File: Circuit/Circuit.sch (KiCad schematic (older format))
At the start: 103 parts, among them SW1 SW_Push, SW10 SW_Push, SW11 SW_Push, SW12 SW_Push, SW13 SW_Push, SW14 SW_Push, SW15 SW_Push, SW16 SW_Push, SW17 SW_Push, SW2 SW_Push, SW3 SW_Push, SW4 SW_Push, SW5 SW_Push, SW6 SW_Push, SW7 SW_Push, SW8 SW_Push, SW9 SW_Push, U1 AD9837, U2 MAX7219

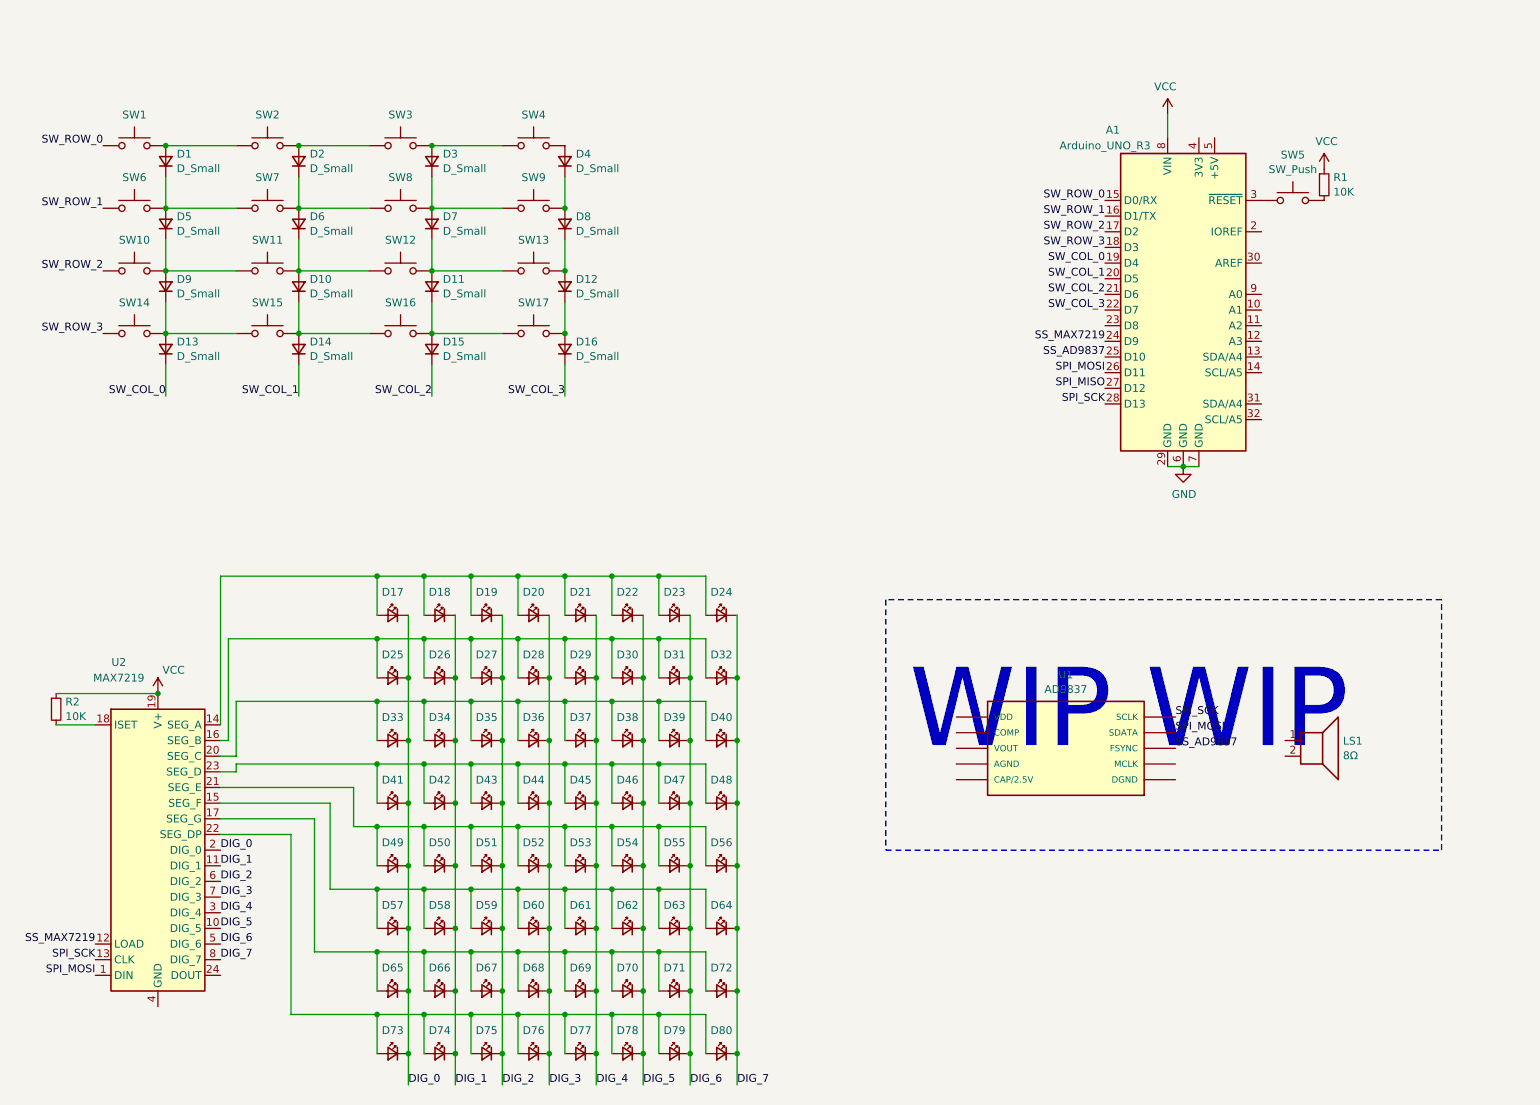
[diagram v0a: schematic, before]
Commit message: Make progress with audio and start laying out PCB.
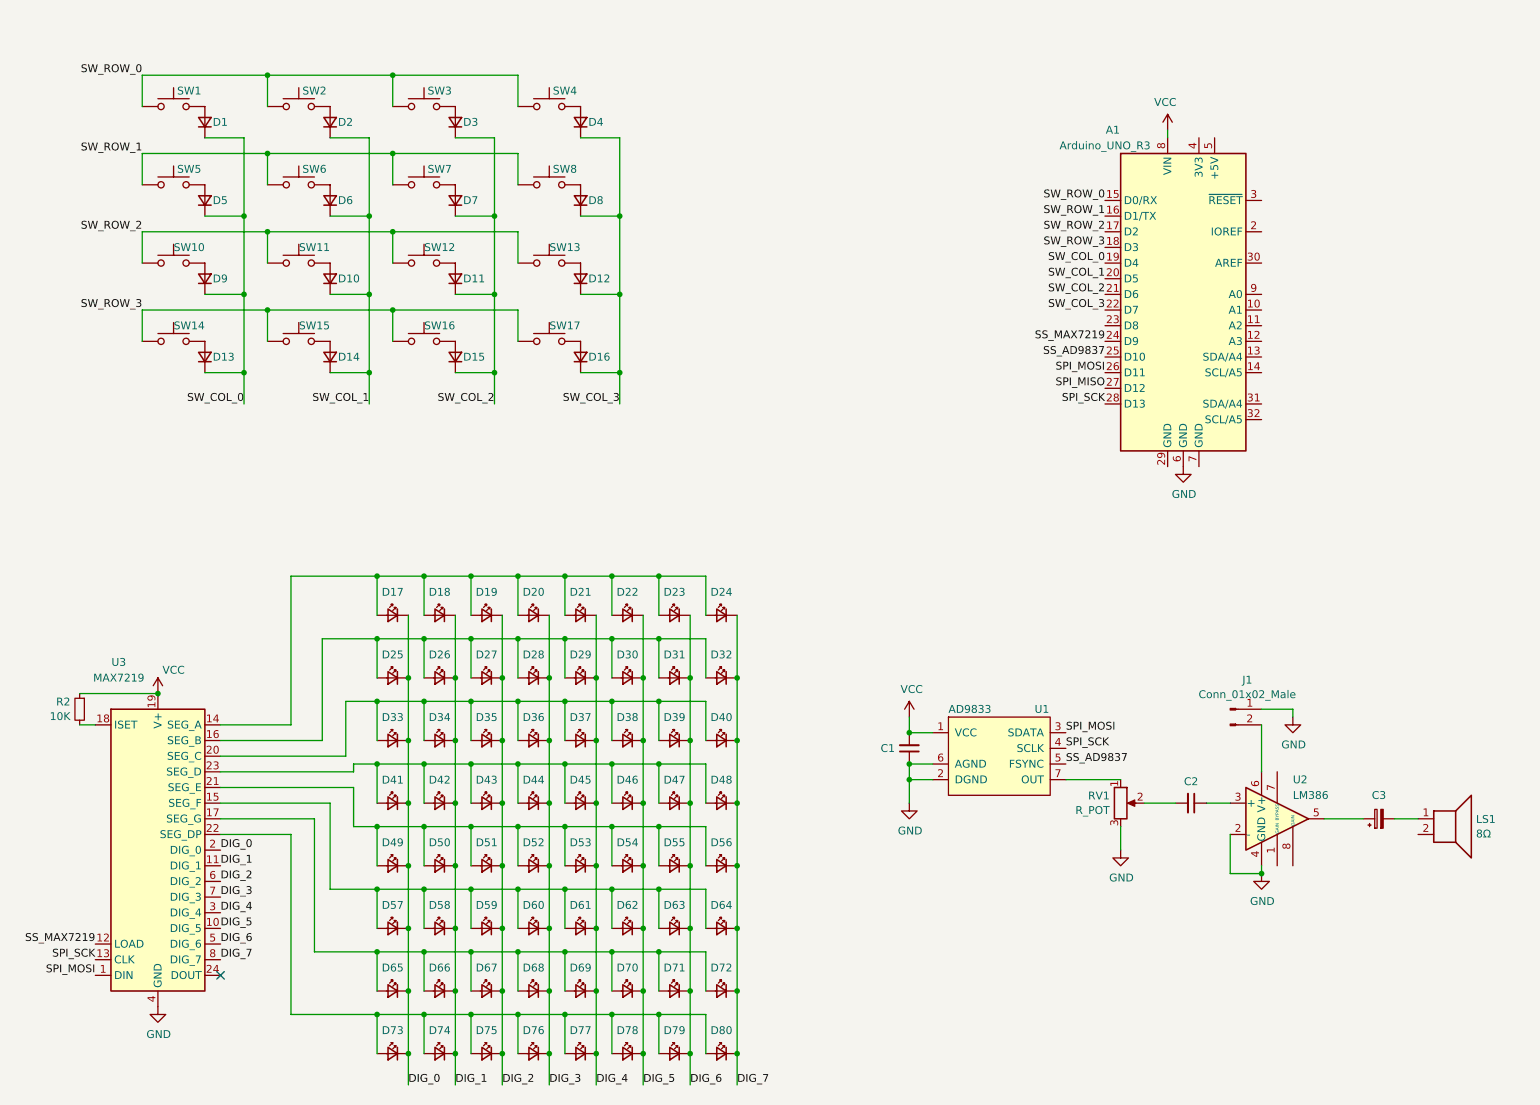
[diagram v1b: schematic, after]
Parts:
- removed R1: 10K, symbol Device:R_Small
- removed SW9: SW_Push, symbol Switch:SW_Push
- removed U1: AD9837, Package_CSP:LFCSP-WD-10-1EP_3x3mm_P0.5mm_EP1.64x2.38mm_ThermalVias, symbol AD9837:AD9837
- added C1, C2: C_Small, symbol Device:C_Small
- added C3: CP_Small, symbol Device:CP_Small
- added J1: Conn_01x02_Male, Connector_PinHeader_2.54mm:PinHeader_1x02_P2.54mm_Vertical, symbol Connector:Conn_01x02_Male
- added RV1: R_POT, Potentiometer_THT:Potentiometer_Vishay_148-149_Single_Horizontal, symbol Device:R_POT
- added U1: AD9833, Connector_PinHeader_2.54mm:PinHeader_1x07_P2.54mm_Vertical, symbol Circuit:AD9833
- added U2: LM386, Package_DIP:DIP-8_W7.62mm_Socket_LongPads, symbol Amplifier_Audio:LM386
- D1, D10, D11, D12, D13, D14, D15, D16, D2, D3, D4, D5, D6, D7, D8, D9: footprint (none) -> Diode_SMD:D_SC-80_HandSoldering
- D17, D18, D19, D20, D21, D22, D23, D24, D25, D26, D27, D28, D29, D30, D31, D32, D33, D34, D35, D36, D37, D38, D39, D40, D41, D42, D43, D44, D45, D46, D47, D48, D49, D50, D51, D52, D53, D54, D55, D56, D57, D58, D59, D60, D61, D62, D63, D64, D65, D66, D67, D68, D69, D70, D71, D72, D73, D74, D75, D76, D77, D78, D79, D80: footprint (none) -> LED_THT:LED_D3.0mm_FlatTop
- R2: footprint (none) -> Resistor_THT:R_Axial_DIN0207_L6.3mm_D2.5mm_P7.62mm_Horizontal
- SW1, SW10, SW11, SW12, SW13, SW14, SW15, SW16, SW17, SW2, SW3, SW4, SW5, SW6, SW7, SW8: footprint (none) -> Button_Switch_Keyboard:SW_Cherry_MX_1.00u_PCB
- U3: renamed from U2; footprint (none) -> Package_DIP:DIP-24_W7.62mm_LongPads
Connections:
- net GND: now also U3.4 (GND), U3.9 (GND), C1.1, J1.1 (Pin_1), RV1.3, U1.2 (DGND), U1.6 (AGND), U2.2 (-), U2.4 (GND); no longer A1.29 (GND), A1.7 (GND)
- net SPI_MOSI: now also U1.3 (SDATA)
- net SPI_SCK: now also U1.4 (SCLK)
- net SS_AD9837: now also U1.5 (FSYNC)
- net SW_COL_0: now also D1.1 (K), D5.1 (K), D9.1 (K)
- net SW_COL_1: now also D10.1 (K), D2.1 (K), D6.1 (K)
- net SW_COL_2: now also D11.1 (K), D3.1 (K), D7.1 (K)
- net SW_COL_3: now also D12.1 (K), D4.1 (K), D8.1 (K)
- net SW_ROW_0: now also SW2.2, SW3.2, SW4.2
- net SW_ROW_1: now also SW5.2, SW7.2, SW8.2
- net SW_ROW_2: now also SW11.2, SW12.2, SW13.2
- net SW_ROW_3: now also SW15.2, SW16.2, SW17.2
- net VCC: now also C1.2, U1.1 (VCC)
- net at D1.2 (A), SW1.1: no longer SW2.2
- net at A1.3 (~RESET): no longer SW5.1
- net at D2.2 (A), SW2.1: no longer SW3.2
- net at D3.2 (A), SW3.1: no longer SW4.2
- net at D8.2 (A): now also SW8.1; no longer D4.1 (K)
- net at D9.2 (A), SW10.1: no longer D5.1 (K), SW11.2
- net at D10.2 (A), SW11.1: no longer D6.1 (K), SW12.2
- net at D11.2 (A), SW12.1: no longer D7.1 (K), SW13.2
- net at D12.2 (A), SW13.1: no longer D8.1 (K)
- net at D13.2 (A), SW14.1: no longer D9.1 (K), SW15.2
- net at D14.2 (A), SW15.1: no longer D10.1 (K), SW16.2
- net at D15.2 (A), SW16.1: no longer D11.1 (K), SW17.2
- net at D16.2 (A), SW17.1: no longer D12.1 (K)
- net at LS1.1: now also C3.2
- new net: C2.1, U2.3 (+)
- new net: C3.1, U2.5
- new net: J1.2 (Pin_2), U2.6 (V+)
- new net: RV1.1, U1.7 (OUT)
- new net: C2.2, RV1.2
- new net: D5.2 (A), SW5.1
- new net: D6.2 (A), SW6.1
- new net: D7.2 (A), SW7.1
- no-connect marks 0 -> 1
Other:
- note removed: "WIP WIP"
- moved on the sheet: LS1, R2

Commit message: Added more traces, added all footprints, and made minor corrections to schematic.
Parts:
- removed J1: Conn_01x02_Male, Connector_PinHeader_2.54mm:PinHeader_1x02_P2.54mm_Vertical, symbol Connector:Conn_01x02_Male
- added BT1: Battery_Cell, Connector_JST:JST_EH_B2B-EH-A_1x02_P2.50mm_Vertical, symbol Device:Battery_Cell
- added C1, C2, C7: 100nF, Capacitor_THT:C_Disc_D4.3mm_W1.9mm_P5.00mm, symbol Device:C_Small
- added C3: 470μF, Capacitor_THT:CP_Radial_D14.0mm_P7.50mm, symbol Device:CP_Small
- added J1: VIN, Connector_PinHeader_2.54mm:PinHeader_1x01_P2.54mm_Vertical, symbol Connector:Conn_01x01_Male
- added J10: SPKR, Connector_PinHeader_2.54mm:PinHeader_1x02_P2.54mm_Vertical, symbol Connector:Conn_01x02_Male
- added J2: 3V3, Connector_PinHeader_2.54mm:PinHeader_1x01_P2.54mm_Vertical, symbol Connector:Conn_01x01_Male
- added J3: LM386 VCC, Connector_PinHeader_2.54mm:PinHeader_1x01_P2.54mm_Vertical, symbol Connector:Conn_01x01_Male
- added J4: BYPASS, Connector_PinHeader_2.54mm:PinHeader_1x01_P2.54mm_Vertical, symbol Connector:Conn_01x01_Male
- added J5: LM386 OUT, Connector_PinHeader_2.54mm:PinHeader_1x01_P2.54mm_Vertical, symbol Connector:Conn_01x01_Male
- added J6: AD9833 OUT, Connector_PinHeader_2.54mm:PinHeader_1x01_P2.54mm_Vertical, symbol Connector:Conn_01x01_Male
- added J7: LM386 IN, Connector_PinHeader_2.54mm:PinHeader_1x03_P2.54mm_Vertical, symbol Connector:Conn_01x03_Male
- added J8: GAIN 1, Connector_PinHeader_2.54mm:PinHeader_1x01_P2.54mm_Vertical, symbol Connector:Conn_01x01_Male
- added J9: GAIN 8, Connector_PinHeader_2.54mm:PinHeader_1x01_P2.54mm_Vertical, symbol Connector:Conn_01x01_Male
- added R2: 10, Resistor_THT:R_Axial_DIN0207_L6.3mm_D2.5mm_P7.62mm_Horizontal, symbol Device:R_Small
- added U1: MicroSDSparkfun, Connector_PinHeader_2.54mm:PinHeader_1x07_P2.54mm_Horizontal, symbol Circuit:MicroSDSparkfun
- C4: renamed from C1; value C_Small -> 100nF; footprint (none) -> Capacitor_THT:C_Disc_D4.3mm_W1.9mm_P5.00mm
- C5: renamed from C2; value C_Small -> 100nF; footprint (none) -> Capacitor_THT:C_Disc_D4.3mm_W1.9mm_P5.00mm
- C6: renamed from C3; value CP_Small -> 470μF; footprint (none) -> Capacitor_THT:CP_Radial_D14.0mm_P7.50mm
- D1, D10, D11, D12, D13, D14, D15, D16, D2, D3, D4, D5, D6, D7, D8, D9: footprint Diode_SMD:D_SC-80_HandSoldering -> Diode_SMD:D_SMB_Handsoldering
- LS1: footprint (none) -> Connector_JST:JST_EH_B2B-EH-A_1x02_P2.50mm_Vertical
- RV1: value R_POT -> 20K
- renumbered R2 to R1, SW11 to SW10, SW12 to SW11, SW13 to SW12, SW14 to SW13, SW15 to SW14, SW16 to SW15, SW17 to SW16, SW10 to SW9, U1 to U2, U2 to U3, U3 to U4
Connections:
- net GND: now also A1.29 (GND), A1.7 (GND), LS1.2, BT1.2 (-), C1.1, C2.1, C3.2, J10.2 (Pin_2), J7.3 (Pin_3), R2.2, U1.7 (GND); no longer U3.2 (-)
- net SPI_MISO: now also U1.5 (MISO)
- net SPI_MOSI: now also U1.3 (MOSI)
- net SPI_SCK: now also U1.4 (SCK)
- net VCC: now also A1.5 (+5V), C1.2, C2.2, U1.1 (VCC); no longer A1.8 (VIN)
- net SS_SDCARD: now reaches A1.23 (D8)
- net SS_SDCARD: now also U1.2 (CS)
- net at A1.4 (3V3): now also J2.1 (Pin_1)
- net SDCARD_CD: now reaches A1.9 (A0)
- net SDCARD_CD: now also U1.6 (CD)
- net at U3.1 (GAIN): now also J8.1 (Pin_1)
- net at C5.1, U3.3 (+): now also J7.1 (Pin_1)
- net at C6.1, U3.5: now also C7.2, J5.1 (Pin_1)
- net +9V: now reaches U3.6 (V+)
- net +9V: now also BT1.1 (+), C3.1, J3.1 (Pin_1)
- net at U3.7 (BYPASS): now also J4.1 (Pin_1)
- net at U3.8 (GAIN): now also J9.1 (Pin_1)
- net at C6.2, LS1.1: now also J10.1 (Pin_1)
- net at RV1.1, U2.7 (OUT): now also J6.1 (Pin_1)
- new net: A1.8 (VIN), J1.1 (Pin_1)
- new net: J7.2 (Pin_2), U3.2 (-)
- new net: C7.1, R2.1
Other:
- moved on the sheet: A1, C4, C5, C6, LS1, RV1, U2, U3

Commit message: Upload final version of Schematic and board layout.
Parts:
- added C2: 100nF, Capacitor_THT:C_Disc_D4.3mm_W1.9mm_P5.00mm, symbol Device:C_Small
- added J3: AREF, Connector_PinHeader_2.54mm:PinHeader_1x01_P2.54mm_Vertical, symbol Connector:Conn_01x01_Male
- added J4: Analog Breakout, Connector_PinHeader_2.54mm:PinHeader_1x05_P2.54mm_Vertical, symbol Connector:Conn_01x05_Male
- added J5: SPI (MOSI, MISO, SCK), Connector_PinHeader_2.54mm:PinHeader_1x03_P2.54mm_Vertical, symbol Connector:Conn_01x03_Male
- added JP1: Jumper, Connector_PinHeader_2.54mm:PinHeader_1x02_P2.54mm_Vertical, symbol Device:Jumper
- J1: value VIN -> POWER; footprint Connector_PinHeader_2.54mm:PinHeader_1x01_P2.54mm_Vertical -> Connector_PinHeader_2.54mm:PinHeader_1x04_P2.54mm_Vertical; symbol Connector:Conn_01x01_Male -> Connector:Conn_01x04_Male
- J2: value 3V3 -> RESET
- renumbered C2 to C5, C5 to C6, C6 to C7, C7 to C8, J7 to J10, J8 to J11, J9 to J12, J10 to J13, J3 to J6, J4 to J7, J5 to J8, J6 to J9
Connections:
- net +9V: now also C2.2
- net GND: now also J1.4 (Pin_4), C2.1
- net SPI_MISO: now also J5.2 (Pin_2)
- net SPI_MOSI: now also J5.1 (Pin_1)
- net SPI_SCK: now also J5.3 (Pin_3)
- net VCC: now also J1.1 (Pin_1)
- net at A1.10 (A1): now also J4.1 (Pin_1)
- net at A1.11 (A2): now also J4.2 (Pin_2)
- net at A1.12 (A3): now also J4.3 (Pin_3)
- net at A1.13 (SDA/A4): now also J4.4 (Pin_4)
- net at A1.14 (SCL/A5): now also J4.5 (Pin_5)
- net at A1.3 (~RESET): now also J2.1 (Pin_1)
- net at A1.30 (AREF): now also J3.1 (Pin_1)
- net at A1.4 (3V3): now also J1.2 (Pin_2); no longer J2.1 (Pin_1)
- net at A1.8 (VIN): now also J1.3 (Pin_3); no longer J1.1 (Pin_1)
- net at C7.1, J8.1 (Pin_1), U3.5: now also JP1.2; no longer C8.2
- new net: C8.2, JP1.1
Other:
- note added: "ROW 0"
- note added: "ROW 1"
- note added: "ROW 2"
- note added: "ROW 3"
- moved on the sheet: BT1, C3, C4, C6, C7, C8, J10, J11, J12, J13, J6, J7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

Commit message: Final touches on circuit.
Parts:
- C8: value 100nF -> 47nF
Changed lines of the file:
@@
 P 9300 5800
 F 0 "C8" H 9400 5750 50  0000 L BNN
-F 1 "100nF" H 9400 5850 50  0000 L CNN
+F 1 "47nF" H 9400 5850 50  0000 L CNN
 F 2 "Capacitor_THT:C_Disc_D4.3mm_W1.9mm_P5.00mm" H 9300 5800 50  0001 C CNN
 F 3 "~" H 9300 5800 50  0001 C CNN
